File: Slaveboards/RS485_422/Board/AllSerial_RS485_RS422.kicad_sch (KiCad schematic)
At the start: 18 parts, among them IC1 7402D, IC2 MAX485CSA, IC3 MAX485CSA, IC4 MAX485CSA, IC5 MAX485CSA, J1 PinHeader_2x05_P2.54mm_Horizo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, X1 ALLSERIALSLAVE, X2 AKL18X-10W

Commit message: improve board/front links
clean up
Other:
- note added: "RS422"
- note added: "XO <- DTR XI -> DSR"
- note added: "XO <- RTS XI -> CTS"
- note removed: "RS485/RS422"
- note removed: "XO = DTR XI = DSR"
- note removed: "XO = RTS XI = CTS"
- moved on the sheet: C1, C2, C3, C4, C5, IC1A, IC1B, IC1C, IC1D, IC1E, IC2A, IC2B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

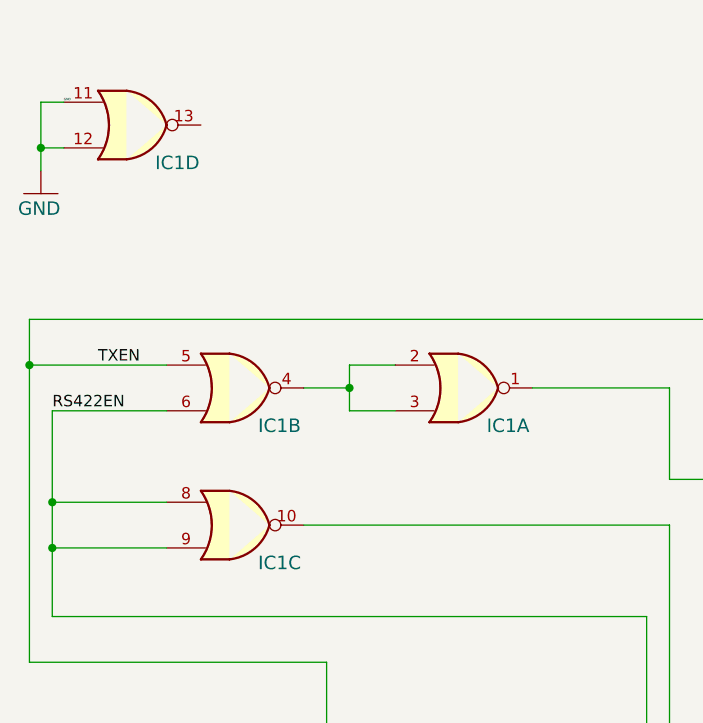
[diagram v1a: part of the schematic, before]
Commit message: Migrate to KiCad 9
Add eBus board
Add various libraries
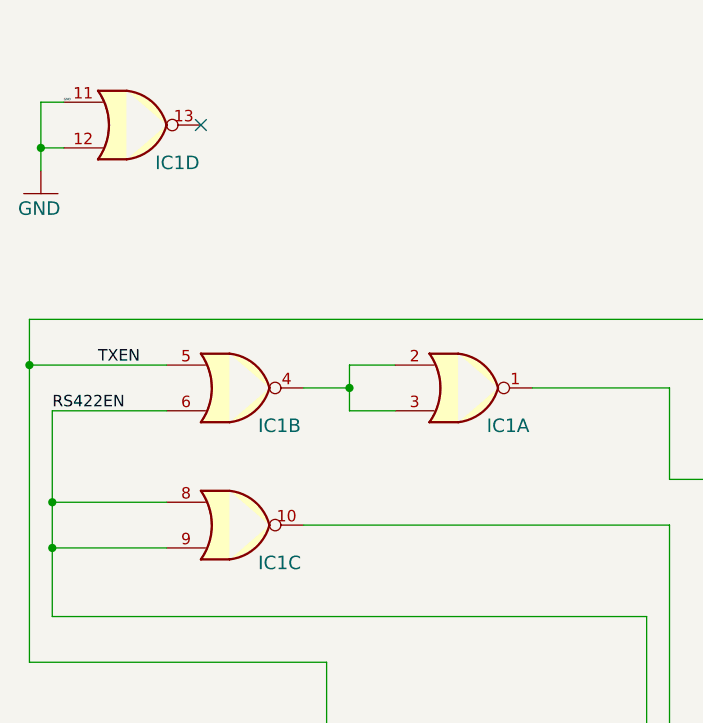
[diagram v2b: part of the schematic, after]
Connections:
- no-connect marks 0 -> 1

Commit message: Improve libraries
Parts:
- added J2: Conn_02x03_Odd_Even, Connector_PinHeader_2.54mm:PinHeader_2x03_P2.54mm_Vertical, symbol Connector_Generic:Conn_02x03_Odd_Even
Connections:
- net at IC4.6 (A), X2.4 (Pin_4): now also J2.5 (Pin_5); no longer R22.1
- net at IC3.7 (B), X2.7 (Pin_7): now also J2.3 (Pin_3); no longer R30.2
- net at IC2.7 (B), X2.9 (Pin_9): now also J2.1 (Pin_1); no longer R5.2
- new net: J2.4 (Pin_4), R30.2
- new net: J2.6 (Pin_6), R22.1
- new net: J2.2 (Pin_2), R5.2
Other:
- moved on the sheet: R22, R30, R5, X2
